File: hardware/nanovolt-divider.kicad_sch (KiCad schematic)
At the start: 11 parts, among them J1 NORMAL IN +, J2 NORMAL IN -, J3 HV IN +, J5 DIVIDER OUT HI, J6 DIVIDER OUT LO, SW1 SW_3PDT NORMAL/HV

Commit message: Swap the TMP117 for a TMP275: SOIC-8, so it can be hand-soldered
The TMP117 only ships as a DSBGA-6 on a 0.4 mm ball pitch, which is not
hand-assemblable, and this board is built by hand. TMP275AIDR is SOIC-8
at 1.27 mm pitch and keeps address 0x48 (A2:A0 all on DGND), so nothing
else on the I2C bus moves.

The cost is absolute accuracy: +/-0.5 C and 12-bit (0.0625 C) instead of
+/-0.1 C and 16-bit (0.0078 C). That is not what this sensor is for - it
tracks the *change* in the 1 ohm region's temperature for the optional
ratio correction, and that needs short-term repeatability, not absolute
accuracy. The register map is not TMP117-compatible, so firmware will
differ when it is written.

Schematic: new project symbol nanovolt-divider:TMP275. KiCad 10 has no
TMP275 - the pinout is the LM75/TMP75 industry-standard one, so
Sensor_Temperature:LM75B would have wired up correctly, but it would put
"LM75B" in the lib_id and call pin 3 "O.S." instead of ALERT. The body is
17.78 mm wide so the rotated V+ / GND pin names clear "ALERT".

Board: a SOIC-8 courtyard is 5.4 mm tall and the band between the
isolation slots and R35 was 5.38 mm, so the sensor no longer fits in the
gap over the resistor body. It sits on the same thermally isolated island
above R35, centred on the resistor's midpoint, 0.7 mm below the slots and
0.8 mm above R35's courtyard - the island is what couples it to R35, not
the millimetre of air over the body. The 1 ohm row dropped 1.5 mm to make
the room, taken from the bottom margin so the slots, the mounting holes
and everything above them stay where the Rev0 review left them.

U2's designator moves to F.Fab and R35's to its pad-1 end (new
REF_OVERRIDE table in gen_pcb.py): there is no silk line left between a
SOIC-8 and a 20 mm resistor sharing a 6.9 mm band. The DSBGA 0.1 mm
intra-footprint DRC exception is gone from the .kicad_dru with the part
that needed it.

ERC 0 violations. The netlist diff is confined to U2's pins. DRC 66
violations against a 67 bas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
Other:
- note added: "1 ohm low leg - TMP275 (U2) mounted adjacent"
- note removed: "1 ohm low leg - TMP117 (U2) mounted adjacent"
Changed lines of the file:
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@@
 	  (property "Footprint" "nanovolt-divider:R_Axial_Vishay_RS02C_L15.1mm_D5.6mm_P20.32mm_Horizontal" (at 289.56 76.2 0) (hide yes) (show_name no) (do_not_autoplace no) (effects (font (size 1.27 1.27)) (justify left)))
 	  (property "Datasheet" "" (at 289.56 76.2 0) (hide yes) (show_name no) (do_not_autoplace no) (effects (font (size 1.27 1.27)) (justify left)))
-	  (property "Description" "Vishay Dale RS-2C wirewound 1 Ohm 1% 2.5 W - shared low leg, never switched; TMP117 adjacent" (at 289.56 76.2 0) (hide yes) (show_name no) (do_not_autoplace no) (effects (font (size 1.27 1.27)) (justify left)))
+	  (property "Description" "Vishay Dale RS-2C wirewound 1 Ohm 1% 2.5 W - shared low leg, never switched; TMP275 adjacent" (at 289.56 76.2 0) (hide yes) (show_name no) (do_not_autoplace no) (effects (font (size 1.27 1.27)) (justify left)))
 	  (property "MPN" "RS02C1R000FE70" (at 289.56 76.2 0) (hide yes) (show_name no) (do_not_autoplace no) (effects (font (size 1.27 1.27)) (justify left)))
 	  (property "Manufacturer" "Vishay Dale" (at 289.56 76.2 0) (hide yes) (show_name no) (do_not_autoplace no) (effects (font (size 1.27 1.27)) (justify left)))
@@
 	(text "Relay states (all relays 2-coil latching, pulsed only):\n  K4 POLARITY : RESET = normal (SRC_P = NORMAL_IN_P), SET = inverted\n  K1..K3 RANGE: SET = range active (one at a time, break-before-make), RESET = open at BOTH ends\n  K5 INJECT   : SET = INJECT (high leg drives 1 ohm), RESET = ISOLATE - both legs open,\n                the source is disconnected from the 1 ohm and the DMM path at both ends\nEach high leg is switched by both poles of its relay: pole A breaks R*_IN, pole B breaks R*_OUT,\nso a deselected resistor is isolated at both ends and never loads RANGE_BUS.\nNominal factor k = 1 / (R_high + 1); actual factors come from calibration.\nNothing switches below the measurement node: the 1 ohm low leg, its pads, and OUT HI/LO are permanent.\nANALOG_RTN / SRC_RTN are never tied to DGND, the control-section ground.\nHV path: 3PDT pole 1 selects the measurement node source, pole 2 selects the return, pole 3 reports the mode.\nHV_IN_P / R34 / SW1 must be rated and laid out for 450 VDC (creepage, clearance, shrouded jacks)." (at 160.02 215.9 0) (effects (font (size 1.27 1.27)) (justify left bottom)))
 	(text "Panel wiring - NOT on the board, so it does not appear in the netlist:\n  HV IN - jack        -> SW1 pole 2, HV lug (lug 6). The board has no HV IN - pad.\n  SW1 pole 3, NORM lug (lug 7) -> unused; R25 (100k, control sheet) already holds HV_SENSE low.\nEvery other SW1 lug lands on a board pad. Confirm the lever-to-throw mapping on the physical\nswitch before wiring: which row is NORMAL depends on the part, which has not been selected yet." (at 160.02 236.22 0) (effects (font (size 1.27 1.27)) (justify left bottom)))
-	(text "1 ohm low leg - TMP117 (U2) mounted adjacent" (at 283 70 0) (effects (font (size 1.0 1.0)) (justify left bottom)))
+	(text "1 ohm low leg - TMP275 (U2) mounted adjacent" (at 283 70 0) (effects (font (size 1.0 1.0)) (justify left bottom)))
 	(sheet_instances (path "/" (page "1")))
 	(embedded_fonts no)

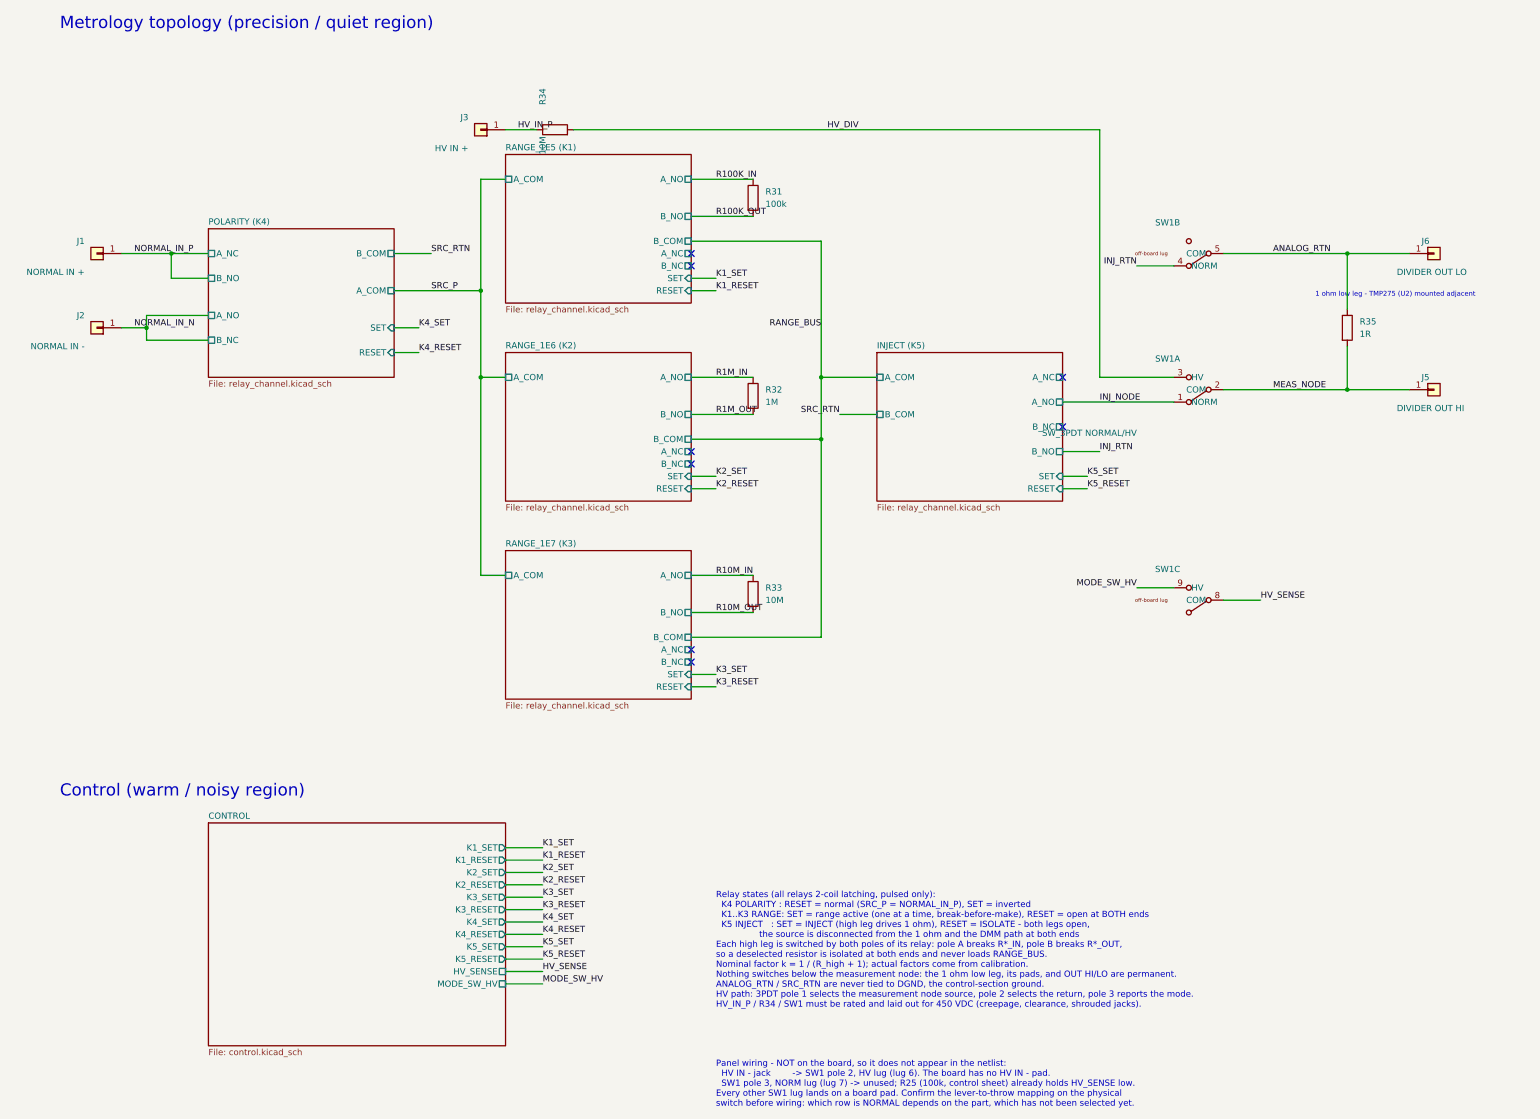
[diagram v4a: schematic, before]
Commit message: Remove the 450 V path: keep the instrument single-purpose
The HV input shared the 1 ohm low leg, and that shared leg capped what the
range could ever be. At 10 M the divider drew 45 uA and gave 45 uV out;
more output meant a smaller high leg, and 1 M draws 450 uA where 10 M
draws 45 uA. A Geiger supply is built to source microamps into a tube that
draws almost none, so its output impedance is high - often set by a series
anode resistor. Against a 1 M source impedance a 10 M divider already
reads 9% low and a 1 M divider reads 50% low, and that error tracks the
supply's operating point, so calibration cannot remove it.

The HV path also had no polarity reversal - K4 serves the NORMAL input
only - so thermal EMF and DMM offset could not be nulled by ABBA the way
they are on the normal ranges. More output was exactly what that path
needed, and the shared 1 ohm leg was the one thing that would not give it.

A dedicated fixed divider has none of those constraints because it picks
its own low leg, so the 450 V measurement moves out of this instrument.

SW1's two analog poles were only ever selecting between the normal path
and the HV path, so with the HV path gone both collapse to plain nets:
K5 A_NO lands directly on MEAS_NODE and B_NO directly on ANALOG_RTN.
ISOLATE is untouched - K5 was always what performed it.

Removed: R34, J3, SW1 and the panel toggle, R24/R25/C5, the J9/P3
harness, the SW_3PDT symbol and its wire-pad footprint, the J_ESP32_P3
symbol and footprint, the HV netclass (generator template and the live
.kicad_pro), and all three HV rules from .kicad_dru - which is now down to
the single bridge-track-width rule. 71 components to 64. The panel is four
banana jacks with nothing wired panel-to-panel, so every conductor now
appears in the netlist.

Board 60 x 94 -> 60 x 83. Getting the full 11 mm needed one extra move:
J1/J2 sat below the relay row, directly above the lower-left mounting
hole, which pinned that hole and through it the slots and the whole 1 oh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
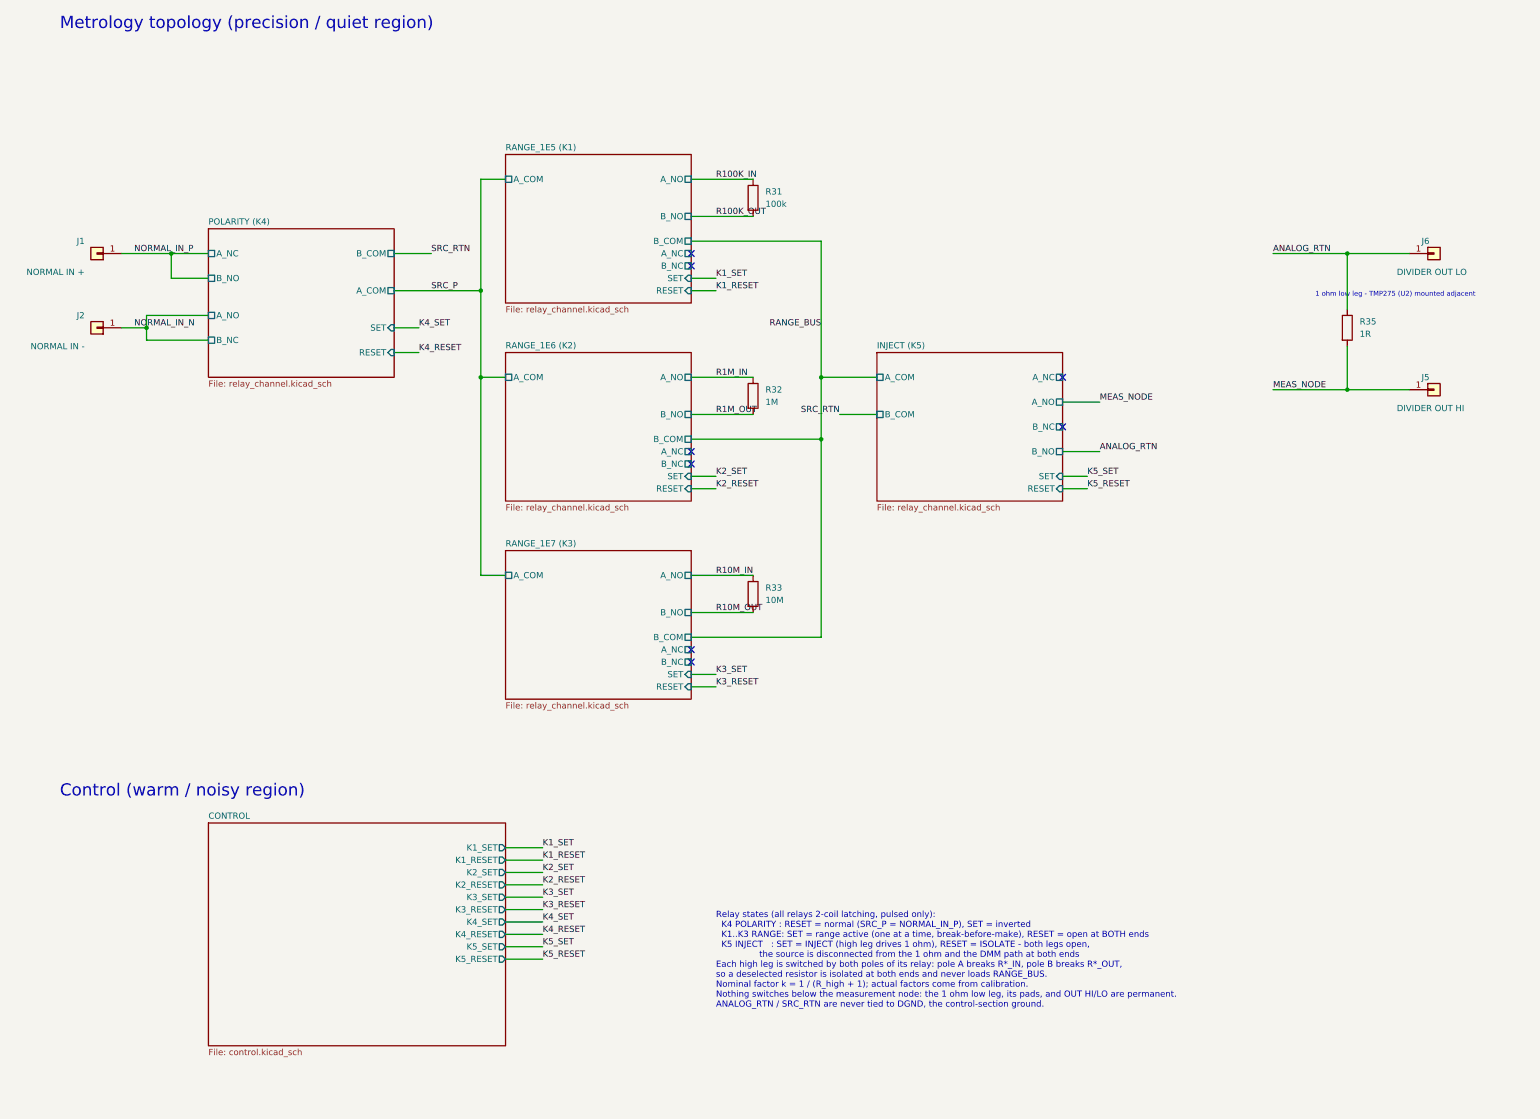
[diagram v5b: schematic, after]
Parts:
- removed J3: HV IN +, Connector_Wire:SolderWire-0.25sqmm_1x01_D0.65mm_OD1.7mm, symbol Connector_Generic:Conn_01x01
- removed R34: 10M, nanovolt-divider:R_Radial_Ohmite_SlimMox_SM102_L14.7mm_W2.5mm_P10.16mm, symbol Device:R
- removed SW1: SW_3PDT NORMAL/HV, nanovolt-divider:SW_3PDT_WirePads_Split, symbol nanovolt-divider:SW_3PDT
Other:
- sheet CONTROL ports: added none; removed HV_SENSE, MODE_SW_HV
- note removed: "Panel wiring - NOT on the board, so it does not appear in the netlist: HV IN - jack -> SW1 pole 2, HV lug (lug 6). The board has no HV IN - pad. SW1 pole 3, NORM lug (lug 7) -> unused; R25 (100k, control sheet) already holds HV_SENSE low. Every other SW1 lug lands on a board pad. Confirm the lever-to-throw mapping on the physical switch before wiring: which row is NORMAL depends on the part, whic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"
